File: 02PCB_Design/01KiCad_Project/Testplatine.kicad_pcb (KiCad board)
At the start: 4 copper layers, 217.9 x 112.1 mm, 143 parts, among them J1 RJ45-8N-B, J2 Screw_Terminal_01x03, J3 FCR7350R, J4 FCR7350R, J5 DE9_Receptacle_MountingHoles, J6 RJ45-8N-B, J7 Conn_01x06_Pin, U1 AS5047P-ATSM, U10 INA240A1PW, U11 NUCLEO-G431RB, U12 MCP2562FD, U2 ISM330BXTR, U3 L6982, U4 AP2114D, U5 LMG2100R044RARR, U6 INA240A1PW, U7 LMG2100R044RARR, U8 INA240A1PW, U9 LMG2100R044RARR

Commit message: All tracks routed
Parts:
- moved J2 3.21 mm to (50.2, 102.2)
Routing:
- net +5V: track 3.73 -> 218.5 mm, vias 13 -> 15
- net +3.3V: track 106.6 -> 244.0 mm, vias 6 -> 8
- net Net-(U11A-PB14): track 6.78 -> 5.18 mm
- net Net-(U12-CANL): track 8.90 -> 7.77 mm
- net /escSheet/Bus_Connectors/IMU_CS: track 64.9 -> 64.3 mm
- net /escSheet/Bus_Connectors/SPI_MOSI: track 31.4 -> 30.8 mm

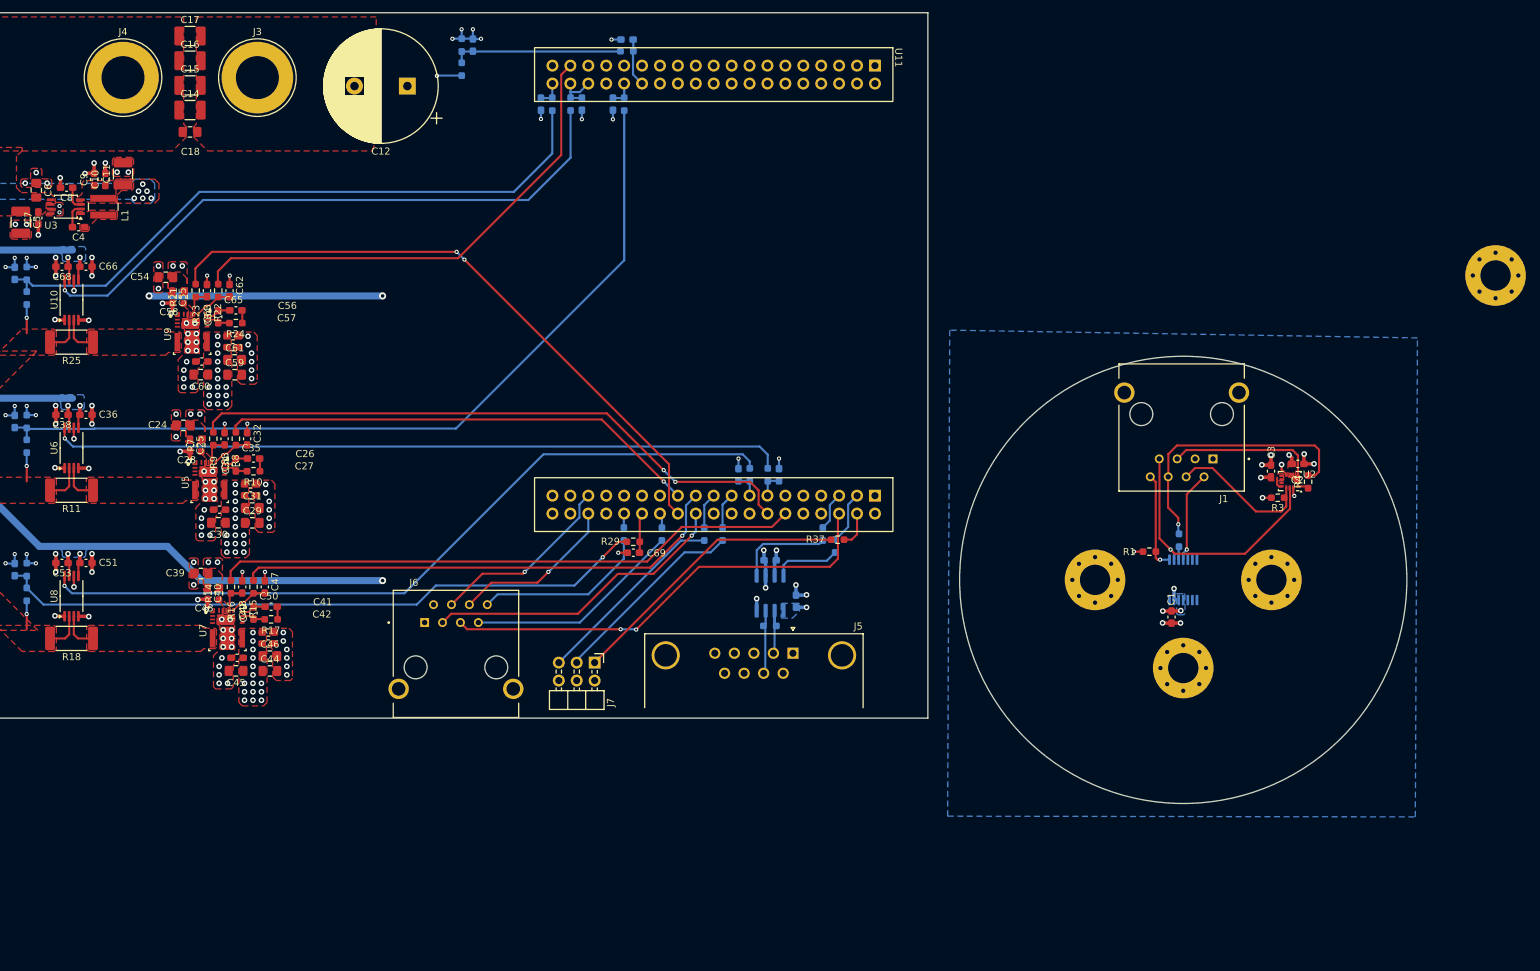
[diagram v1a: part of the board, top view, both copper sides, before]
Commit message: edited footprints
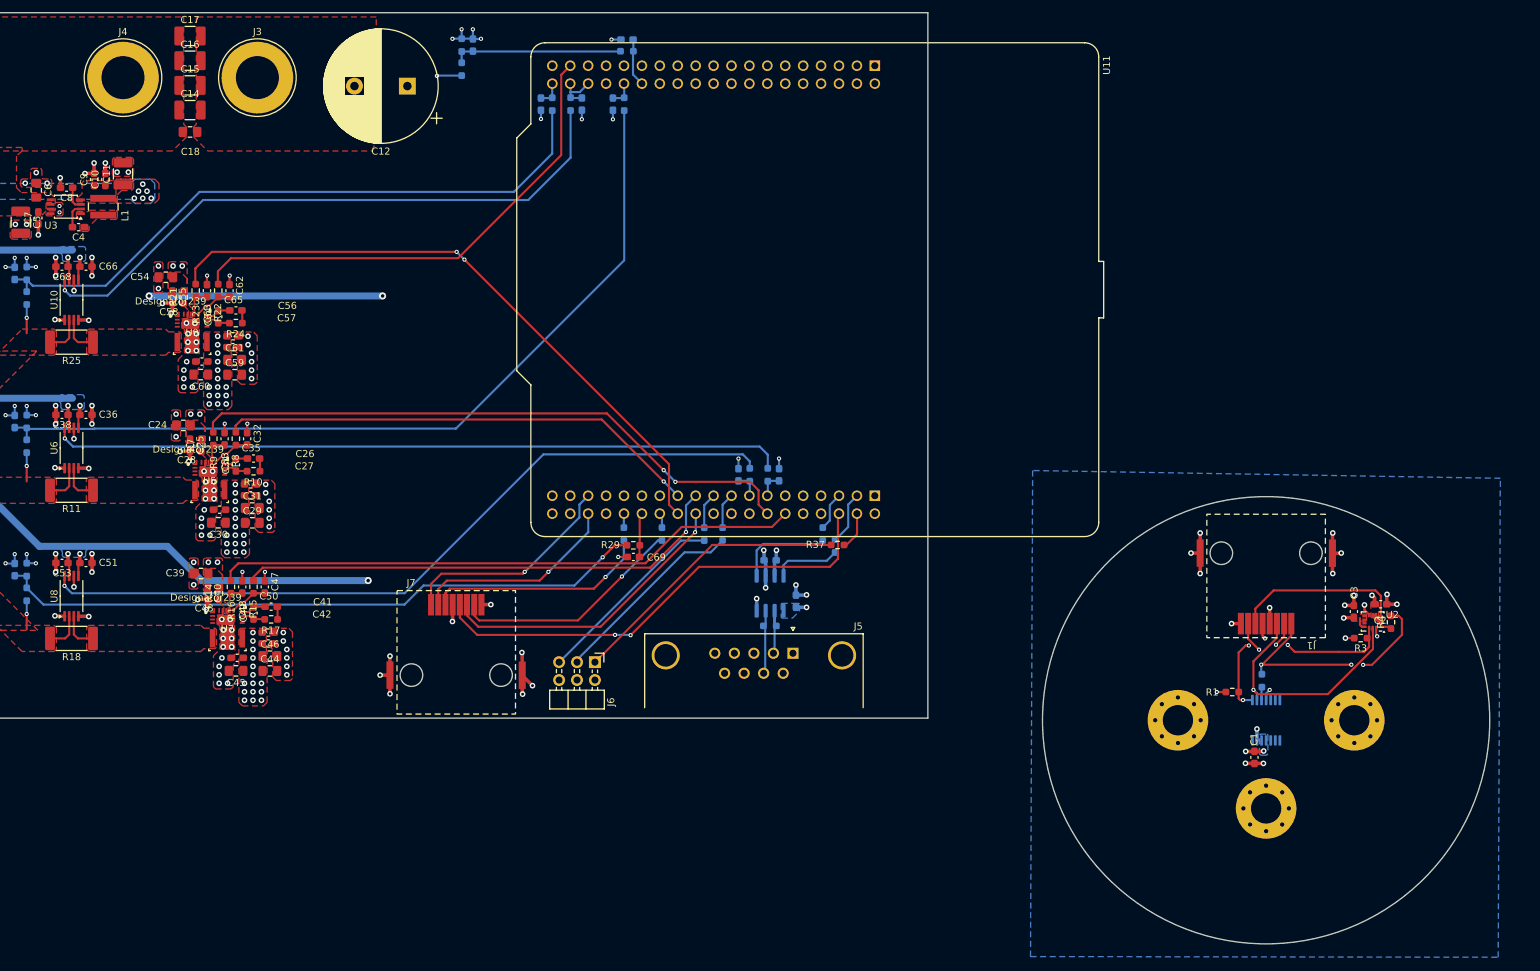
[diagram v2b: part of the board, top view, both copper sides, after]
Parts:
- removed H4: MountingHole, MountingHole:MountingHole_4.3mm_M4_Pad_Via
- H1, H2, H3: value MountingHole -> MountingHole_Pad
- J1: footprint RJ45-8N-B:TE_RJ45-8N-B -> MyFootprintLib:Wurth_634008_RJ45
- J6: value RJ45-8N-B -> Conn_01x06_Pin; footprint RJ45-8N-B:TE_RJ45-8N-B -> Connector_PinHeader_2.54mm:PinHeader_2x03_P2.54mm_Horizontal
- J7: value Conn_01x06_Pin -> RJ45-8N-B; footprint Connector_PinHeader_2.54mm:PinHeader_2x03_P2.54mm_Horizontal -> MyFootprintLib:Wurth_634008_RJ45
- U11: footprint footprints:NucleoMorphoG431RB -> MyFootprintLib:NucleoCN7CN10
- U5, U7, U9: footprint footprints:RAR0016B-MFG -> MyFootprintLib:RAR0016B-MFG
- moved H1 66.2 mm to (254.2, 139.9)
- moved J1 32.0 mm to (241.8, 126.2)
- moved U2 23.1 mm to (256.9, 125.9)
- moved C1 23.1 mm to (240.1, 145.2)
- moved C3 23.1 mm to (254.2, 124.5)
- moved H2 23.1 mm to (241.8, 152.4)
- moved H3 23.1 mm to (229.2, 139.9)
- moved R1 23.1 mm to (237.0, 135.9)
- moved R4 23.1 mm to (259.5, 126.0)
- moved U1 23.1 mm to (241.8, 139.9)
- moved C2 23.1 mm to (258.0, 123.5)
- moved R2 23.1 mm to (241.2, 134.3)
- moved R3 23.1 mm to (255.2, 128.3)
- moved J7 21.3 mm to (126.9, 123.5), turned to 0 degrees
- moved J6 19.7 mm to (146.6, 131.7), turned to -90 degrees
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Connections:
- H1 pad 1: (no net) -> GND1
- H2 pad 1: (no net) -> GND1
- H3 pad 1: (no net) -> GND1
- J1 pad 1: +3.3VP -> (no net)
- J1 pad 2: /SensorSheet/SPI_MOSI -> (no net)
- J1 pad 3: GND1 -> (no net)
- J1 pad 4: /SensorSheet/IMU_CS -> (no net)
- J1 pad 5: /SensorSheet/IMU_INT1 -> (no net)
- J1 pad 6: /SensorSheet/SPI_MISO -> (no net)
- J1 pad 7: /SensorSheet/SPI_SCLK -> (no net)
- J1 pad 8: /SensorSheet/ENC_CS -> (no net)
- J6 pad 1: +3.3V -> /escSheet/Bus_Connectors/O_ENC_A
- J6 pad 2: unconnected-(J6-Pad2) -> GNDA
- J6 pad 3: /escSheet/Bus_Connectors/IMU_INT1 -> /escSheet/Bus_Connectors/O_ENC_I
- J6 pad 4: /escSheet/Bus_Connectors/SPI_MISO -> +3.3V
- J6 pad 5: /escSheet/Bus_Connectors/IMU_CS -> /escSheet/Bus_Connectors/O_ENC_B
- J6 pad 6: /escSheet/Bus_Connectors/ENC_CS -> +5V
- J7 pad 1: /escSheet/Bus_Connectors/O_ENC_A -> +3.3V
- J7 pad 2: GNDA -> /escSheet/Bus_Connectors/SPI_MOSI
- J7 pad 3: /escSheet/Bus_Connectors/O_ENC_I -> /escSheet/Bus_Connectors/IMU_INT1
- J7 pad 4: +3.3V -> /escSheet/Bus_Connectors/IMU_CS
- J7 pad 5: /escSheet/Bus_Connectors/O_ENC_B -> GNDA
- J7 pad 6: +5V -> /escSheet/Bus_Connectors/SPI_SCLK
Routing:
- net GNDA: track 106.8 -> 123.9 mm, vias 151 -> 158
- net (no net): track 0.00 -> 14.1 mm, vias 0 -> 6
- net +3.3V: track 244.0 -> 251.2 mm, vias 8 -> 9
- net /escSheet/Bus_Connectors/SPI_SCLK: track 24.6 -> 31.5 mm, vias 0 -> 1
- net /escSheet/Bus_Connectors/ENC_CS: track 23.7 -> 29.5 mm
- net /escSheet/Bus_Connectors/SPI_MISO: track 26.9 -> 31.5 mm
- net /SensorSheet/SPI_MISO: track 38.9 -> 34.8 mm, vias 1 -> 3
- net /SensorSheet/ENC_CS: track 13.9 -> 17.8 mm, vias 1 -> 3
- net /SensorSheet/IMU_INT1: track 20.8 -> 24.2 mm
- net /escSheet/Bus_Connectors/IMU_CS: track 64.3 -> 67.2 mm
- net /SensorSheet/SPI_SCLK: track 38.0 -> 35.3 mm
- net /escSheet/Bus_Connectors/SPI_MOSI: track 30.8 -> 33.1 mm, vias 0 -> 1
- net GND1: track 11.3 -> 13.6 mm, vias 8 -> 9
- net +3.3VP: track 12.3 -> 13.6 mm, vias 6 -> 7
- net /escSheet/Bus_Connectors/IMU_INT1: track 43.8 -> 42.8 mm
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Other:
- board size 217.9 x 112.1 mm -> 229.7 x 132 mm

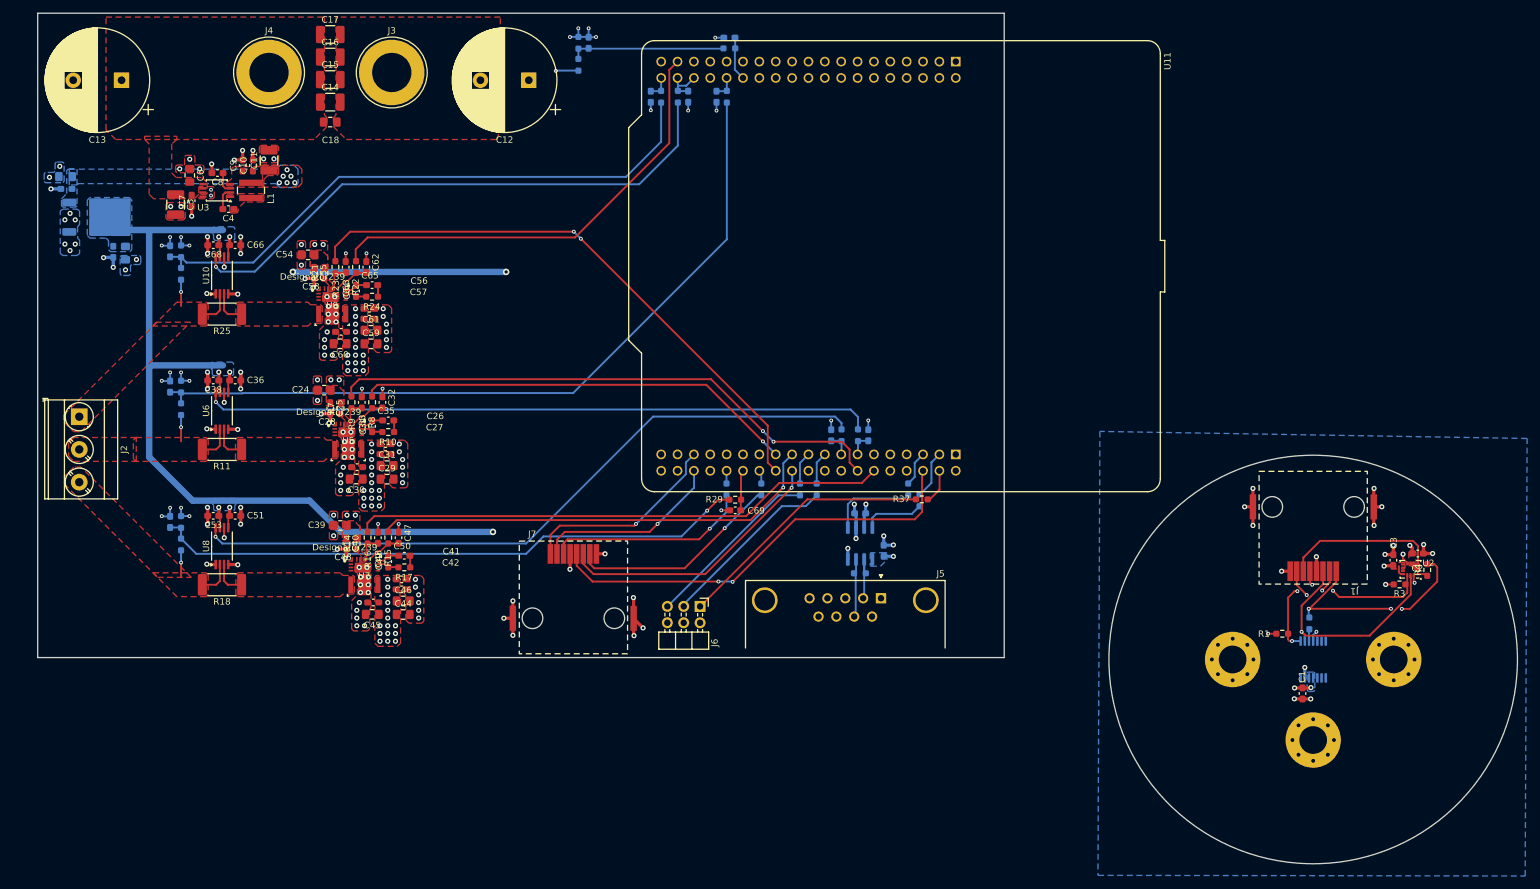
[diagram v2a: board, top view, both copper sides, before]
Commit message: Via stitching and edited footprints
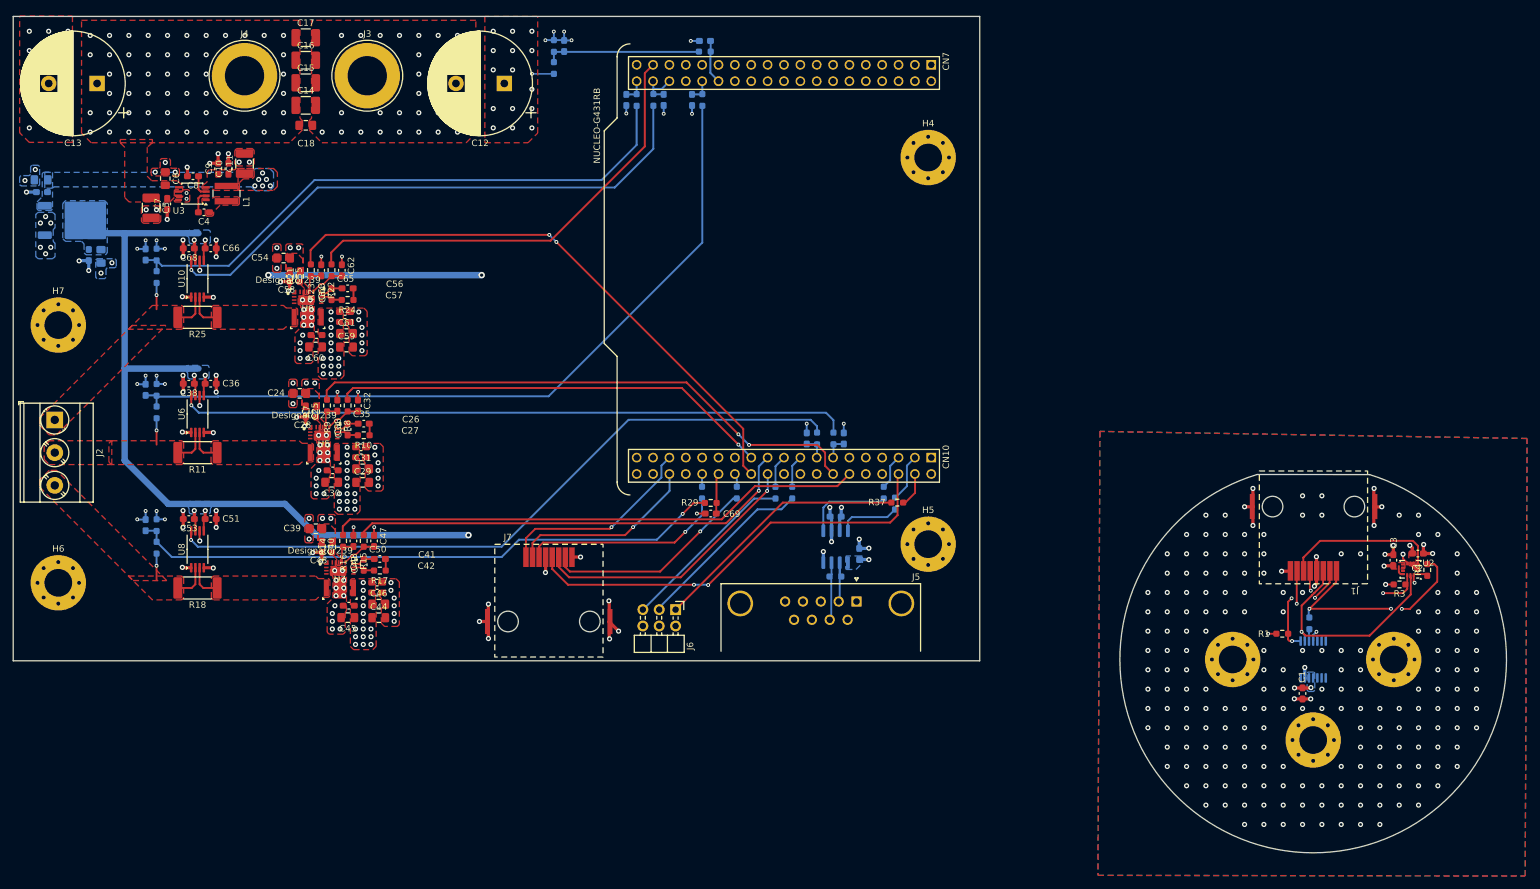
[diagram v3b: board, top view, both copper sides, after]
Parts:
- added H4: MountingHole, MountingHole:MountingHole_4.3mm_M4_Pad_Via, F.Cu at (182.0, 62.0)
- added H5: MountingHole, MountingHole:MountingHole_4.3mm_M4_Pad_Via, F.Cu at (182.0, 122.0)
- added H6: MountingHole, MountingHole:MountingHole_4.3mm_M4_Pad_Via, F.Cu at (47.0, 128.0)
- added H7: MountingHole, MountingHole:MountingHole_4.3mm_M4_Pad_Via, F.Cu at (47.0, 88.0)
- moved C23 3.83 mm to (125.5, 44.7)
- moved C29 3.83 mm to (94.2, 112.4)
- moved C31 3.83 mm to (94.2, 110.3)
- moved C44 3.83 mm to (96.7, 133.4)
- moved C46 3.83 mm to (96.7, 131.3)
- moved C59 3.83 mm to (91.7, 91.4)
- moved C61 3.83 mm to (91.7, 89.3)
- moved C69 3.83 mm to (148.2, 117.2)
- moved C71 3.83 mm to (140.9, 53.0)
- moved C72 3.83 mm to (147.3, 43.9)
- moved C73 3.83 mm to (145.3, 53.1)
- moved C77 3.83 mm to (167.6, 117.7)
- moved C9 3.83 mm to (71.8, 63.7)
- moved J5 3.83 mm to (170.9, 130.9)
- moved R11 3.83 mm to (68.6, 107.8)
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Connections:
- J1 pad 1: (no net) -> +3.3VP
- J1 pad 2: (no net) -> /SensorSheet/SPI_MOSI
- J1 pad 3: (no net) -> /SensorSheet/IMU_INT1
- J1 pad 4: (no net) -> /SensorSheet/IMU_CS
- J1 pad 5: (no net) -> GND1
- J1 pad 6: (no net) -> /SensorSheet/SPI_SCLK
- J1 pad 7: (no net) -> /SensorSheet/ENC_CS
- J1 pad 8: (no net) -> /SensorSheet/SPI_MISO
- J1 pad SHIELD: (no net) -> GND1
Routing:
- net +3.3VP: track 13.6 -> 77.8 mm
- net GND1: track 13.6 -> 30.1 mm, vias 9 -> 203
- net (no net): track 14.1 -> 0.00 mm, vias 6 -> 0
- net +24V: track 3.53 -> 3.42 mm, vias 46 -> 115
- net GNDA: vias 158 -> 203
- added copper zone on F.Cu, net GND1
- added copper zone on In2.Cu, net GND1
- removed copper zone on In2.Cu, net +3.3VP
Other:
- board size 229.7 x 132 mm -> 231.7 x 129.8 mm
